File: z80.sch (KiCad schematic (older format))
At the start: 9 parts, among them P1 CONN_02X20

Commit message: * added USB data signals to first slot * added logo to the top of the board. * added logo PNG files.
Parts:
- added P2: CONN_01X02, Socket_Strips:Socket_Strip_Straight_1x02, symbol CONN_01X02
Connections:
- wire segments 128 -> 132
- no-connect marks 3 -> 1
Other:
- note added: "place next to\ncard slot #1"
- moved on the sheet: C11, USB1
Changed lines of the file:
@@
 $EndDescr
 $Sheet
-S 3050 1900 550  4300
+S 3050 1900 550  4400
 U 577A9E9B
 F0 "CPU" 60
@@
 	4100 6000 4200 6100
 $Sheet
-S 4650 1900 550  4300
+S 4650 1900 550  4400
 U 577F17CE
 F0 "Card Slots" 60
@@
 L USB_B USB1
 U 1 1 57951B8F
-P 9650 1000
-F 0 "USB1" H 9850 800 50  0000 C CNN
-F 1 "USB_B" H 9600 1200 50  0000 C CNN
-F 2 "Connect:USB_B" V 9600 900 50  0001 C CNN
-F 3 "" V 9600 900 50  0000 C CNN
-	1    9650 1000
+P 9550 750
+F 0 "USB1" H 9750 550 50  0000 C CNN
+F 1 "USB_B" H 9500 950 50  0000 C CNN
+F 2 "Connect:USB_B" V 9500 650 50  0001 C CNN
+F 3 "" V 9500 650 50  0000 C CNN
+	1    9550 750
 	1    0    0    -1
 $EndComp
@@
 L GND #PWR01
 U 1 1 57953BC6
-P 9750 1900
-F 0 "#PWR01" H 9750 1650 50  0001 C CNN
-F 1 "GND" H 9750 1750 50  0000 C CNN
-F 2 "" H 9750 1900 50  0000 C CNN
-F 3 "" H 9750 1900 50  0000 C CNN
-	1    9750 1900
-	1    0    0    -1
-$EndComp
-Wire Wire Line
-	9750 1300 9750 1900
+P 9650 2000
+F 0 "#PWR01" H 9650 1750 50  0001 C CNN
+F 1 "GND" H 9650 1850 50  0000 C CNN
+F 2 "" H 9650 2000 50  0000 C CNN
+F 3 "" H 9650 2000 50  0000 C CNN
+	1    9650 2000
+	1    0    0    -1
+$EndComp
+Wire Wire Line
+	9650 1050 9650 2000
 $Comp
 L VCC #PWR02
 U 1 1 57955ECB
-P 9200 1250
-F 0 "#PWR02" H 9200 1100 50  0001 C CNN
-F 1 "VCC" H 9200 1400 50  0000 C CNN
-F 2 "" H 9200 1250 50  0000 C CNN
-F 3 "" H 9200 1250 50  0000 C CNN
-	1    9200 1250
-	1    0    0    -1
-$EndComp
-Wire Wire Line
-	9450 1300 9450 1500
+P 9100 1000
+F 0 "#PWR02" H 9100 850 50  0001 C CNN
+F 1 "VCC" H 9100 1150 50  0000 C CNN
+F 2 "" H 9100 1000 50  0000 C CNN
+F 3 "" H 9100 1000 50  0000 C CNN
+	1    9100 1000
+	1    0    0    -1
+$EndComp
+Wire Wire Line
+	9350 1050 9350 1600
 $Comp
 L CP C11
 U 1 1 57964E06
-P 9450 1650
-F 0 "C11" H 9475 1750 50  0000 L CNN
-F 1 "10u" H 9475 1550 50  0000 L CNN
-F 2 "Capacitors_ThroughHole:C_Radial_D6.3_L11.2_P2.5" H 9488 1500 50  0001 C CNN
-F 3 "" H 9450 1650 50  0000 C CNN
-	1    9450 1650
-	1    0    0    -1
-$EndComp
-Connection ~ 9450 1400
-Wire Wire Line
-	9450 1800 9450 1850
-Wire Wire Line
-	9450 1850 10000 1850
-Connection ~ 9750 1850
-NoConn ~ 9550 1300
-NoConn ~ 9650 1300
-NoConn ~ 9950 900
-Text Notes 9150 700  0    60   ~ 0
+P 9350 1750
+F 0 "C11" H 9375 1850 50  0000 L CNN
+F 1 "10u" H 9375 1650 50  0000 L CNN
+F 2 "Capacitors_ThroughHole:C_Radial_D6.3_L11.2_P2.5" H 9388 1600 50  0001 C CNN
+F 3 "" H 9350 1750 50  0000 C CNN
+	1    9350 1750
+	1    0    0    -1
+$EndComp
+Connection ~ 9350 1500
+Wire Wire Line
+	9350 1900 9350 1950
+Wire Wire Line
+	9350 1950 9900 1950
+Connection ~ 9650 1950
+NoConn ~ 9850 650
+Text Notes 8300 700  0    60   ~ 0
 USB power source
 Wire Notes Line
@@
 	6300 2200 6300 500
 Wire Wire Line
-	9200 1250 9200 1400
+	9100 1000 9100 1500
 $Comp
 L PWR_FLAG #FLG05
 U 1 1 57951B7E
-P 10000 1750
-F 0 "#FLG05" H 10000 1845 50  0001 C CNN
-F 1 "PWR_FLAG" H 10000 1930 50  0000 C CNN
-F 2 "" H 10000 1750 50  0000 C CNN
-F 3 "" H 10000 1750 50  0000 C CNN
-	1    10000 1750
-	1    0    0    -1
-$EndComp
-Wire Wire Line
-	10000 1850 10000 1750
-Wire Wire Line
-	9200 1400 9450 1400
+P 9900 1850
+F 0 "#FLG05" H 9900 1945 50  0001 C CNN
+F 1 "PWR_FLAG" H 9900 2030 50  0000 C CNN
+F 2 "" H 9900 1850 50  0000 C CNN
+F 3 "" H 9900 1850 50  0000 C CNN
+	1    9900 1850
+	1    0    0    -1
+$EndComp
+Wire Wire Line
+	9900 1950 9900 1850
+Wire Wire Line
+	9100 1500 9350 1500
 Wire Bus Line
 	2500 1500 5750 1500
@@
 Wire Wire Line
 	6800 3750 7550 3750
+Wire Wire Line
+	9550 1050 9550 1200
+Wire Wire Line
+	9450 1300 10400 1300
+Wire Wire Line
+	9450 1300 9450 1050
+$Comp
+L CONN_01X02 P2
+U 1 1 57A5699E
+P 10600 1250
+F 0 "P2" H 10600 1400 50  0000 C CNN
+F 1 "CONN_01X02" V 10700 1250 50  0000 C CNN
+F 2 "Socket_Strips:Socket_Strip_Straight_1x02" H 10600 1250 50  0001 C CNN
+F 3 "" H 10600 1250 50  0000 C CNN
+	1    10600 1250
+	1    0    0    -1
+$EndComp
+Text Notes 10350 950  0    60   ~ 0
+place next to\ncard slot #1
+Wire Wire Line
+	9550 1200 10400 1200
 $EndSCHEMATC

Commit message: * Replaced one card slot with an updated expansion connector. * Replaced '138 with GAL. * Implemented interrupt priority lines IEI/IEO. * Replaced discrete oscillator with 14/8 pin DIP oscillator block.
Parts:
- removed P1: CONN_02X20, Socket_Strips:Socket_Strip_Angled_2x20, symbol CONN_02X20
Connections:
- wire segments 132 -> 86

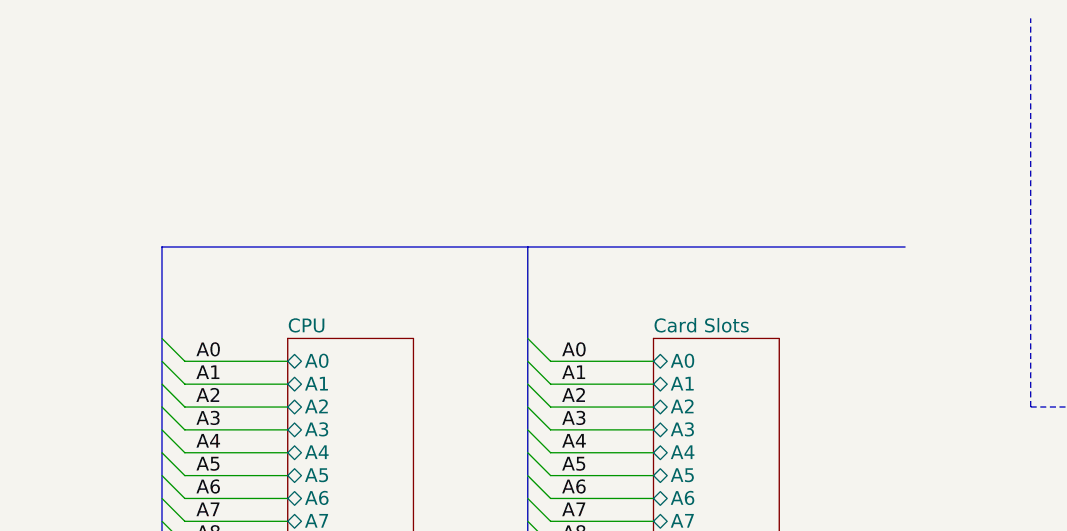
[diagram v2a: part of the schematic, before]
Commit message: Fixed schema DRC errors
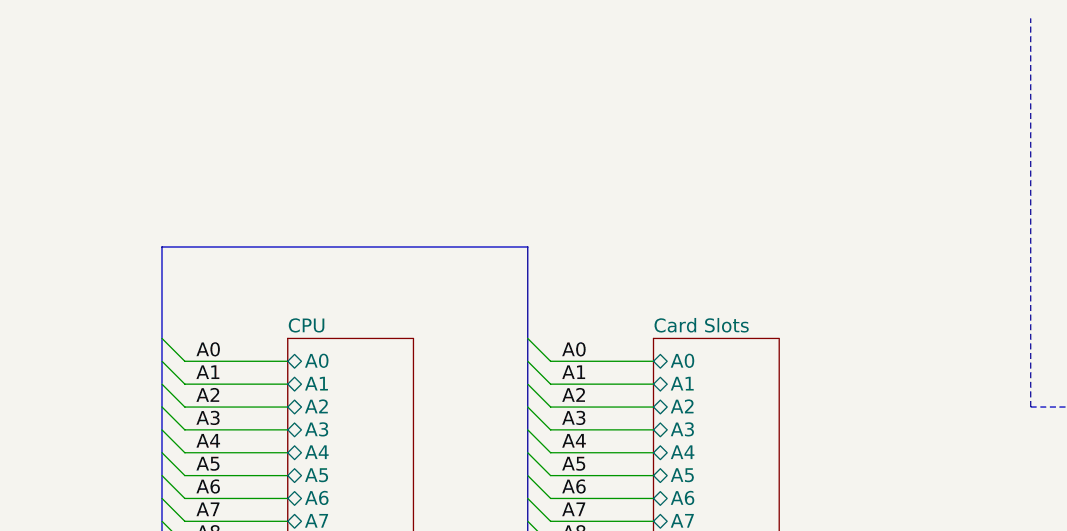
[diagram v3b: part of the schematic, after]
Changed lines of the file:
@@
 $EndComp
 $Comp
-L GND #PWR8
+L GND #PWR01
 U 1 1 57953BC6
 P 9650 2000
-F 0 "#PWR8" H 9650 1750 50  0001 C CNN
+F 0 "#PWR01" H 9650 1750 50  0001 C CNN
 F 1 "GND" H 9650 1850 50  0000 C CNN
 F 2 "" H 9650 2000 50  0000 C CNN
@@
 	9650 1050 9650 2000
 $Comp
-L VCC #PWR7
+L VCC #PWR02
 U 1 1 57955ECB
 P 9100 1000
-F 0 "#PWR7" H 9100 850 50  0001 C CNN
+F 0 "#PWR02" H 9100 850 50  0001 C CNN
 F 1 "VCC" H 9100 1150 50  0000 C CNN
 F 2 "" H 9100 1000 50  0000 C CNN
@@
 $EndComp
 $Comp
-L GND #PWR4
+L GND #PWR03
 U 1 1 5799297A
 P 6600 1950
-F 0 "#PWR4" H 6600 1700 50  0001 C CNN
+F 0 "#PWR03" H 6600 1700 50  0001 C CNN
 F 1 "GND" H 6600 1800 50  0000 C CNN
 F 2 "" H 6600 1950 50  0000 C CNN
@@
 	6600 1850 6600 1950
 $Comp
-L VCC #PWR3
+L VCC #PWR04
 U 1 1 5799477B
 P 6600 950
-F 0 "#PWR3" H 6600 800 50  0001 C CNN
+F 0 "#PWR04" H 6600 800 50  0001 C CNN
 F 1 "VCC" H 6600 1100 50  0000 C CNN
 F 2 "" H 6600 950 50  0000 C CNN
@@
 	9100 1000 9100 1500
 $Comp
-L PWR_FLAG #FLG1
+L PWR_FLAG #FLG05
 U 1 1 57951B7E
 P 9900 1850
-F 0 "#FLG1" H 9900 1945 50  0001 C CNN
+F 0 "#FLG05" H 9900 1945 50  0001 C CNN
 F 1 "PWR_FLAG" H 9900 2030 50  0000 C CNN
 F 2 "" H 9900 1850 50  0000 C CNN
@@
 Wire Wire Line
 	9100 1500 9350 1500
-Wire Bus Line
-	2500 1500 5750 1500
 Wire Wire Line
 	9550 1050 9550 1200
@@
 Wire Wire Line
 	9550 1200 10400 1200
+Wire Bus Line
+	2500 1500 4100 1500
 $EndSCHEMATC

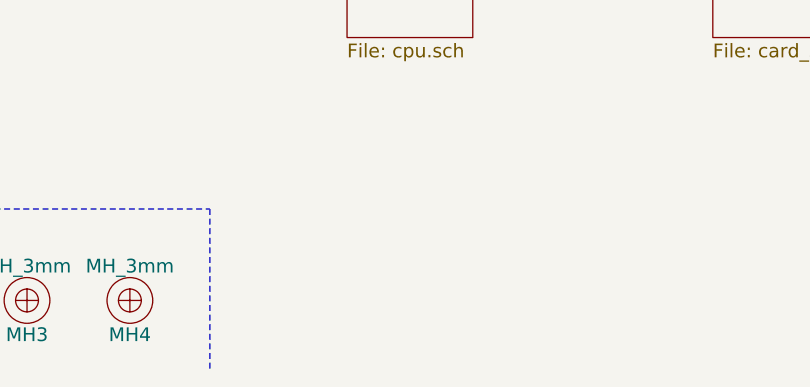
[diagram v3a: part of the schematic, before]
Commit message: Added logo schematic elements and new logo for bottom side.
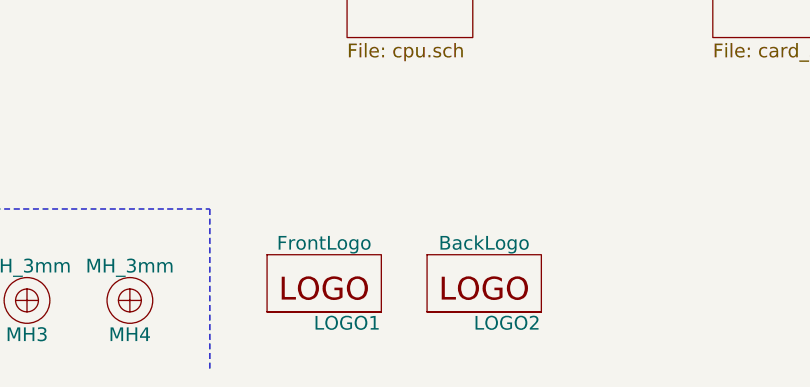
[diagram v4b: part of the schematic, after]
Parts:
- added LOGO1: FrontLogo, ncr2016_logo:nrc2016_top_logo_1600, symbol FrontLogo
- added LOGO2: BackLogo, ncr2016_logo:nrc2016_top_logo_1600, symbol FrontLogo
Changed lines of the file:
@@
 LIBS:atf16v8cv
 LIBS:62256
+LIBS:mcp2221a
 LIBS:z80-cache
 EELAYER 25 0
@@
 Wire Bus Line
 	2500 1500 4100 1500
+$Comp
+L FrontLogo LOGO1
+U 1 1 57B3A1A4
+P 2700 7500
+F 0 "LOGO1" H 3050 7450 60  0000 C CNN
+F 1 "FrontLogo" H 2950 7800 60  0000 C CNN
+F 2 "ncr2016_logo:nrc2016_top_logo_1600" H 2700 7500 60  0001 C CNN
+F 3 "" H 2700 7500 60  0000 C CNN
+	1    2700 7500
+	1    0    0    -1
+$EndComp
+$Comp
+L FrontLogo LOGO2
+U 1 1 57B3B1B1
+P 3400 7500
+F 0 "LOGO2" H 3750 7450 60  0000 C CNN
+F 1 "BackLogo" H 3650 7800 60  0000 C CNN
+F 2 "ncr2016_logo:nrc2016_top_logo_1600" H 3400 7500 60  0001 C CNN
+F 3 "" H 3400 7500 60  0000 C CNN
+	1    3400 7500
+	1    0    0    -1
+$EndComp
 $EndSCHEMATC

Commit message: Dunno what changed. . ?
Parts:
- LOGO2: footprint ncr2016_logo:nrc2016_top_logo_1600 -> ncr2016_logo:nrc2016_bottom_logo_600
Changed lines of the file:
@@
 F 0 "LOGO2" H 3750 7450 60  0000 C CNN
 F 1 "BackLogo" H 3650 7800 60  0000 C CNN
-F 2 "ncr2016_logo:nrc2016_top_logo_1600" H 3400 7500 60  0001 C CNN
+F 2 "ncr2016_logo:nrc2016_bottom_logo_600" H 3400 7500 60  0001 C CNN
 F 3 "" H 3400 7500 60  0000 C CNN
 	1    3400 7500

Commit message: * fixed DRC errors on pin 1 of Px2 connectors. * fixed unconnected ground pin issue of GAL. * added 8DIP and 14DIP oscillator block footprint. * updated bottom silkscreen. * added via stitching in a few places for better GND net. * routed the reset and oscillator circuits. * Design passes KiCAD DRC.
!! This is NRC016 RC1 !!
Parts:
- LOGO2: footprint ncr2016_logo:nrc2016_bottom_logo_600 -> ncr2016_logo:nrc2016_bottom_logo_600_v2
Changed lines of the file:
@@
 F 0 "LOGO2" H 3750 7450 60  0000 C CNN
 F 1 "BackLogo" H 3650 7800 60  0000 C CNN
-F 2 "ncr2016_logo:nrc2016_bottom_logo_600" H 3400 7500 60  0001 C CNN
+F 2 "ncr2016_logo:nrc2016_bottom_logo_600_v2" H 3400 7500 60  0001 C CNN
 F 3 "" H 3400 7500 60  0000 C CNN
 	1    3400 7500
